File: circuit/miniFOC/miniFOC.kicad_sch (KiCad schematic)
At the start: 0 parts

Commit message: The design of the miniFOC circuit schematic is basically completed.
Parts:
- added C?: 22uF, Capacitor_SMD:C_0603_1608Metric_Pad1.08x0.95mm_HandSolder, symbol Device:C
- added C? (x4): 330pF, Capacitor_SMD:C_0402_1005Metric, symbol Device:C
- added C? (x3): 1uF, Capacitor_SMD:C_0402_1005Metric, symbol Device:C
- added C?: 4.7uF, Capacitor_SMD:C_1206_3216Metric_Pad1.33x1.80mm_HandSolder, symbol Device:C
- added C?: 100nF, Capacitor_SMD:C_0603_1608Metric_Pad1.08x0.95mm_HandSolder, symbol Device:C
- added C?: 10uF, Capacitor_SMD:C_1206_3216Metric_Pad1.33x1.80mm_HandSolder, symbol Device:C
- added C? (x2): 10uF, Capacitor_SMD:C_0603_1608Metric_Pad1.08x0.95mm_HandSolder, symbol Device:C
- added C?: 100nF, Capacitor_SMD:C_0402_1005Metric, symbol Device:C
- added D? (x3): B0530W, Diode_SMD:D_SOD-123, symbol Diode:1N4148W
- added L?: 4.7uH, PowerLibrary:IND-SMD_L4.6-W4.2_SMMS0420, symbol Device:L
- added Q? (x6): AP30H50Q, Package_SON:VSON-8_3.3x3.3mm_P0.65mm_NexFET, symbol Library:AP30H50Q
- added R? (x2): 20mR, Resistor_SMD:R_0805_2012Metric, symbol Device:R
- added R? (x4): 1kR, Resistor_SMD:R_0402_1005Metric, symbol Device:R
- added R? (x4): 15kR, Resistor_SMD:R_0402_1005Metric, symbol Device:R
- added R?: 100kR, Resistor_SMD:R_0603_1608Metric_Pad0.98x0.95mm_HandSolder, symbol Device:R
- added R?: 10kR, Resistor_SMD:R_0402_1005Metric, symbol Device:R
- added R?: 3kR, Resistor_SMD:R_0603_1608Metric_Pad0.98x0.95mm_HandSolder, symbol Device:R
- added R?: 16kR, Resistor_SMD:R_0603_1608Metric_Pad0.98x0.95mm_HandSolder, symbol Device:R
- added U?: COS722MR, Package_SO:MSOP-8_3x3mm_P0.65mm, symbol Library:COS722MR
- added U?: AT32F421C8, Package_QFP:LQFP-48_7x7mm_P0.5mm, symbol Library:AT32F421C8
- added U?: EG2133, Package_SO:TSSOP-20_4.4x6.5mm_P0.65mm, symbol Library:EG2133
- added U?: JW5017S, Package_TO_SOT_SMD:SOT-23-6, symbol power_Library:JW5017S
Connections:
- new net: C?.1, R?.1, R?.2, U?.5 (IN2+)
- new net: C?.1, R?.1, R?.1, U?.3 (IN1+)
- new net: C?.2, R?.2, R?.2, U?.2 (IN1-)
- new net: C?.1, L?.1, U?.6 (SW)
- new net: C?.2, U?.1 (BST)
- new net: R?.1, U?.4 (EN)
- new net: C?.2, R?.1, R?.2, U?.6 (IN2-)
- new net: R?.2, R?.2, U?.3 (FB)
- new net +15V: C?.2, C?.2, Q?.5 (D), Q?.5 (D), Q?.5 (D), R?.2, U?.5 (VIN)
- new net +3.3V: R?.1, U?.1 (VDD), U?.24 (VDD), U?.48 (VDD), U?.9 (VDDA)
- new net +5V: C?.2, C?.2, C?.2, D?.2 (A), D?.2 (A), D?.2 (A), L?.2, R?.1, U?.7 (VCC), U?.8 (VDD)
- new net ADC1_CH0: C?.1, R?.1, U?.1 (OUTA), U?.10 (PA0)
- new net ADC1_CH1: C?.1, R?.1, U?.11 (PA1), U?.7 (OUTB)
- new net ADC1_CH2: U?.12 (PA2)
- new net GND: C?.1, C?.1, C?.1, C?.1, C?.1, C?.2, Q?.1 (S), Q?.2 (S), Q?.3 (S), R?.1, R?.1, R?.2, R?.2, R?.2, U?.2 (GND), U?.23 (VSS), U?.4 (VSS), U?.47 (VSS), U?.8 (GND), U?.8 (VSSA)
- new net HO1: Q?.4 (G), U?.19 (HO1)
- new net HO2: Q?.4 (G), U?.16 (HO2)
- new net HO3: Q?.4 (G), U?.13 (HO3)
- new net LO1: Q?.4 (G), U?.11 (LO1)
- new net LO2: Q?.4 (G), U?.10 (LO2)
- new net LO3: Q?.4 (G), U?.9 (LO3)
- new net NRST: C?.1, R?.2, U?.7 (NRST)
- new net SA1_P: Q?.1 (S), Q?.2 (S), Q?.3 (S), R?.1, R?.2
- new net SA2_P: Q?.1 (S), Q?.2 (S), Q?.3 (S), R?.1, R?.1
- new net SPI_CLK: U?.15 (PA5)
- new net SPI_CS: U?.14 (PA4)
- new net SPI_MISO: U?.16 (PA6)
- new net SWDCLK: U?.37 (SWCLK)
- new net SWDIO: U?.34 (SWDIO)
- new net TIM1_CH1: U?.1 (HIN1), U?.29 (PA8), U?.4 (~{LIN1})
- new net TIM1_CH2: U?.2 (HIN2), U?.30 (PA9), U?.5 (~{LIN2})
- new net TIM1_CH3: U?.3 (HIN3), U?.31 (PA10), U?.6 (~{LIN3})
- new net USART1_RX: U?.43 (PB7)
- new net USART1_TX: U?.42 (PB6)
- new net VAA: C?.2, C?.2, R?.2, R?.2
- new net VB1: C?.1, D?.1 (K), U?.20 (VB1)
- new net VB2: C?.1, D?.1 (K), U?.17 (VB2)
- new net VB3: C?.1, D?.1 (K), U?.14 (VB3)
- new net VS1: C?.2, Q?.1 (S), Q?.2 (S), Q?.3 (S), Q?.5 (D), U?.18 (VS1)
- new net VS2: C?.2, Q?.1 (S), Q?.2 (S), Q?.3 (S), Q?.5 (D), U?.15 (VS2)
- new net VS3: C?.2, Q?.1 (S), Q?.2 (S), Q?.3 (S), Q?.5 (D), U?.12 (VS3)
- no-connect marks 0 -> 27
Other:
- note added: "Driver"
- note added: "MCU"
- note added: "Power"
- note added: "Sample"

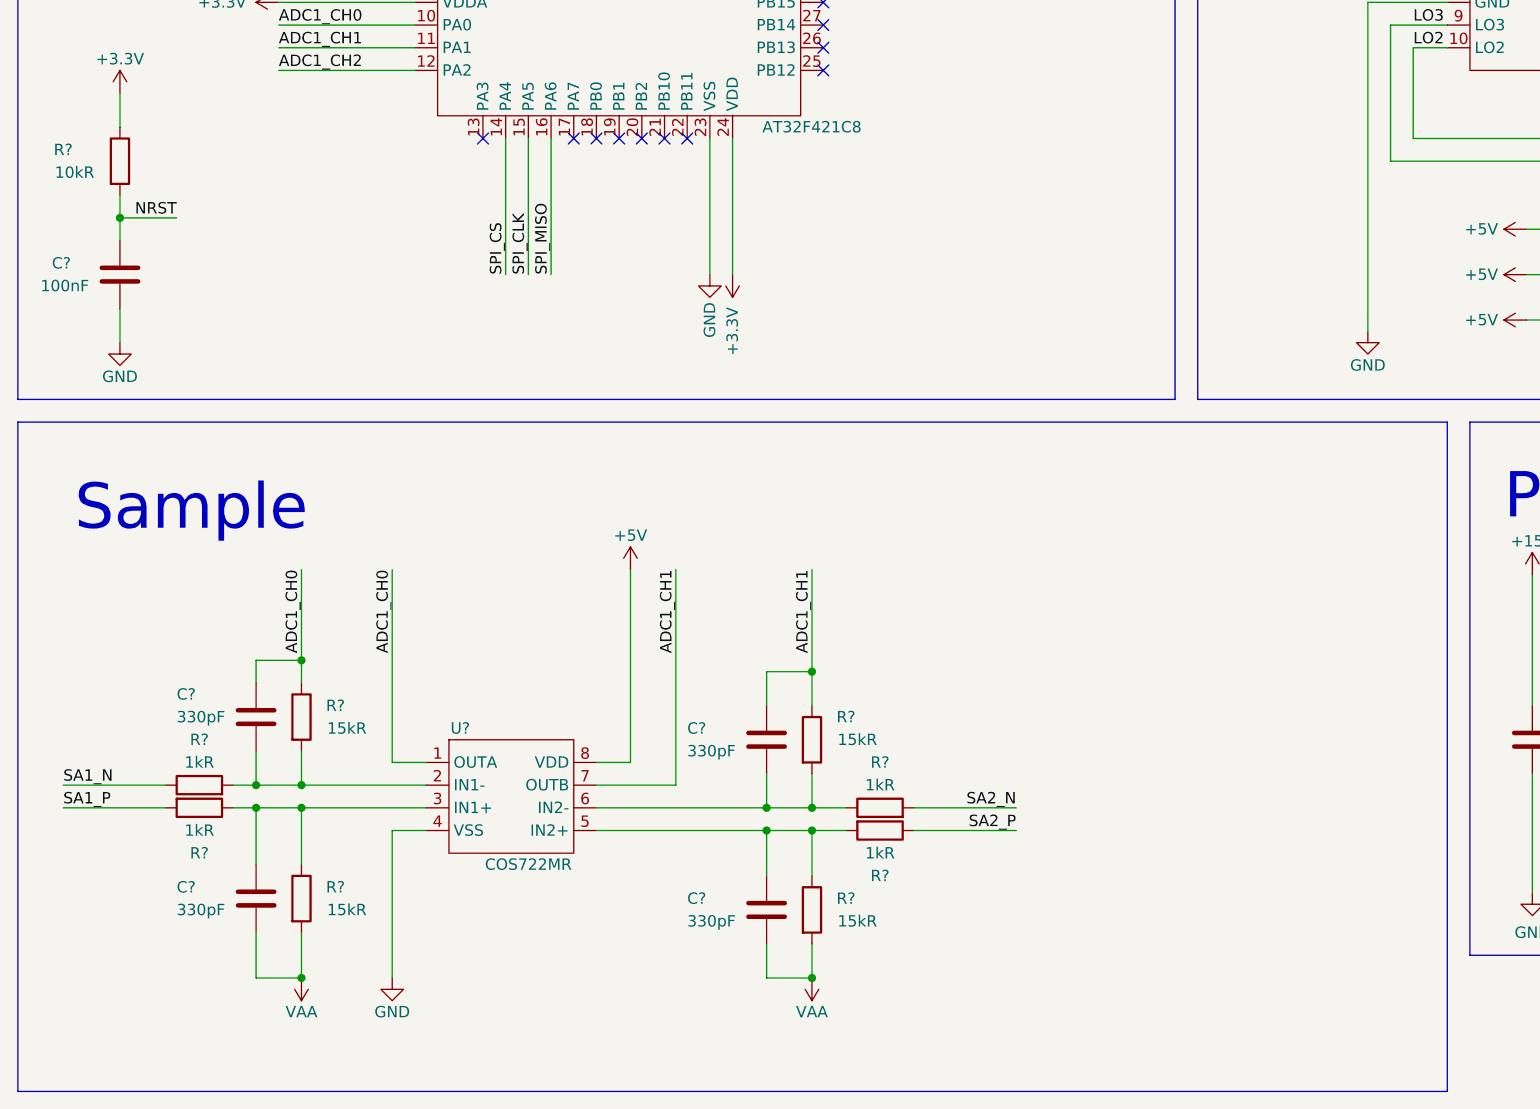
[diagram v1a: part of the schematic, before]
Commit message: Modify the op-amp symbol to triangle.
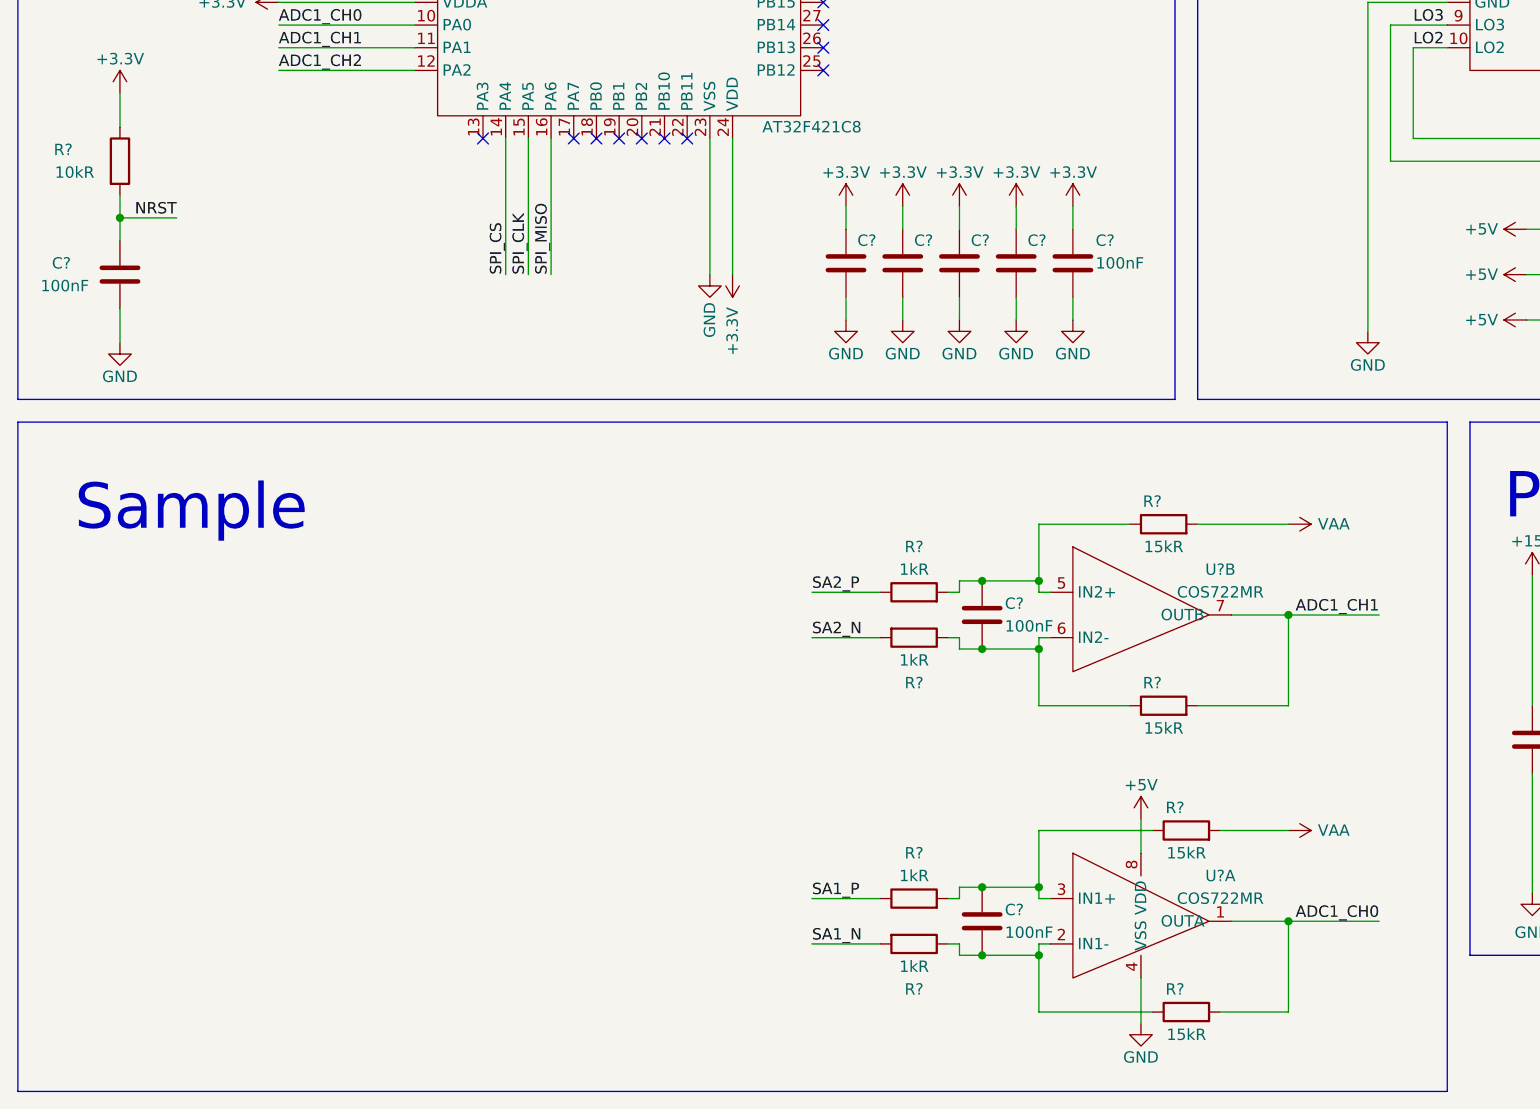
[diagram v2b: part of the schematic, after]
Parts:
- removed C? (x4): 330pF, Capacitor_SMD:C_0402_1005Metric, symbol Device:C
- removed R? (x2): 1kR, Resistor_SMD:R_0402_1005Metric, symbol Device:R
- removed R? (x3): 15kR, Resistor_SMD:R_0402_1005Metric, symbol Device:R
- removed U?: COS722MR, Package_SO:MSOP-8_3x3mm_P0.65mm, symbol Library:COS722MR
- added C? (x7): 100nF, Capacitor_SMD:C_0402_1005Metric, symbol Device:C
- added R? (x3): 15kR, Resistor_SMD:R_0402_1005Metric, symbol Device:R
- added R? (x2): 1kR, Resistor_SMD:R_0402_1005Metric, symbol Device:R
- added U? (x2): COS722MR, Package_SO:MSOP-8_3x3mm_P0.65mm, symbol Library:COS722MR
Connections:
- net +3.3V: now also C?.1, C?.1, C?.1, C?.1, C?.1
- net +5V: now also U?.8 (VDD)
- net ADC1_CH0: now also R?.2, U?.1 (OUTA)
- net ADC1_CH1: now also R?.2, U?.7 (OUTB)
- net GND: now also R?.2, C?.2, C?.2, C?.2, C?.2, C?.2, R?.2, U?.4 (VSS); no longer R?.1
- net SA1_P: now also R?.1; no longer R?.2
- net SA2_P: now also R?.1
- net VAA: now also R?.2, R?.2; no longer R?.2
- net at R?.1, R?.1: now also C?.2, U?.2 (IN1-)
- net at R?.2: now also C?.1, R?.1, U?.3 (IN1+)
- new net: C?.1, R?.1, R?.2, U?.5 (IN2+)
- new net: C?.2, R?.1, R?.1, U?.6 (IN2-)
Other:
- moved on the sheet: R?

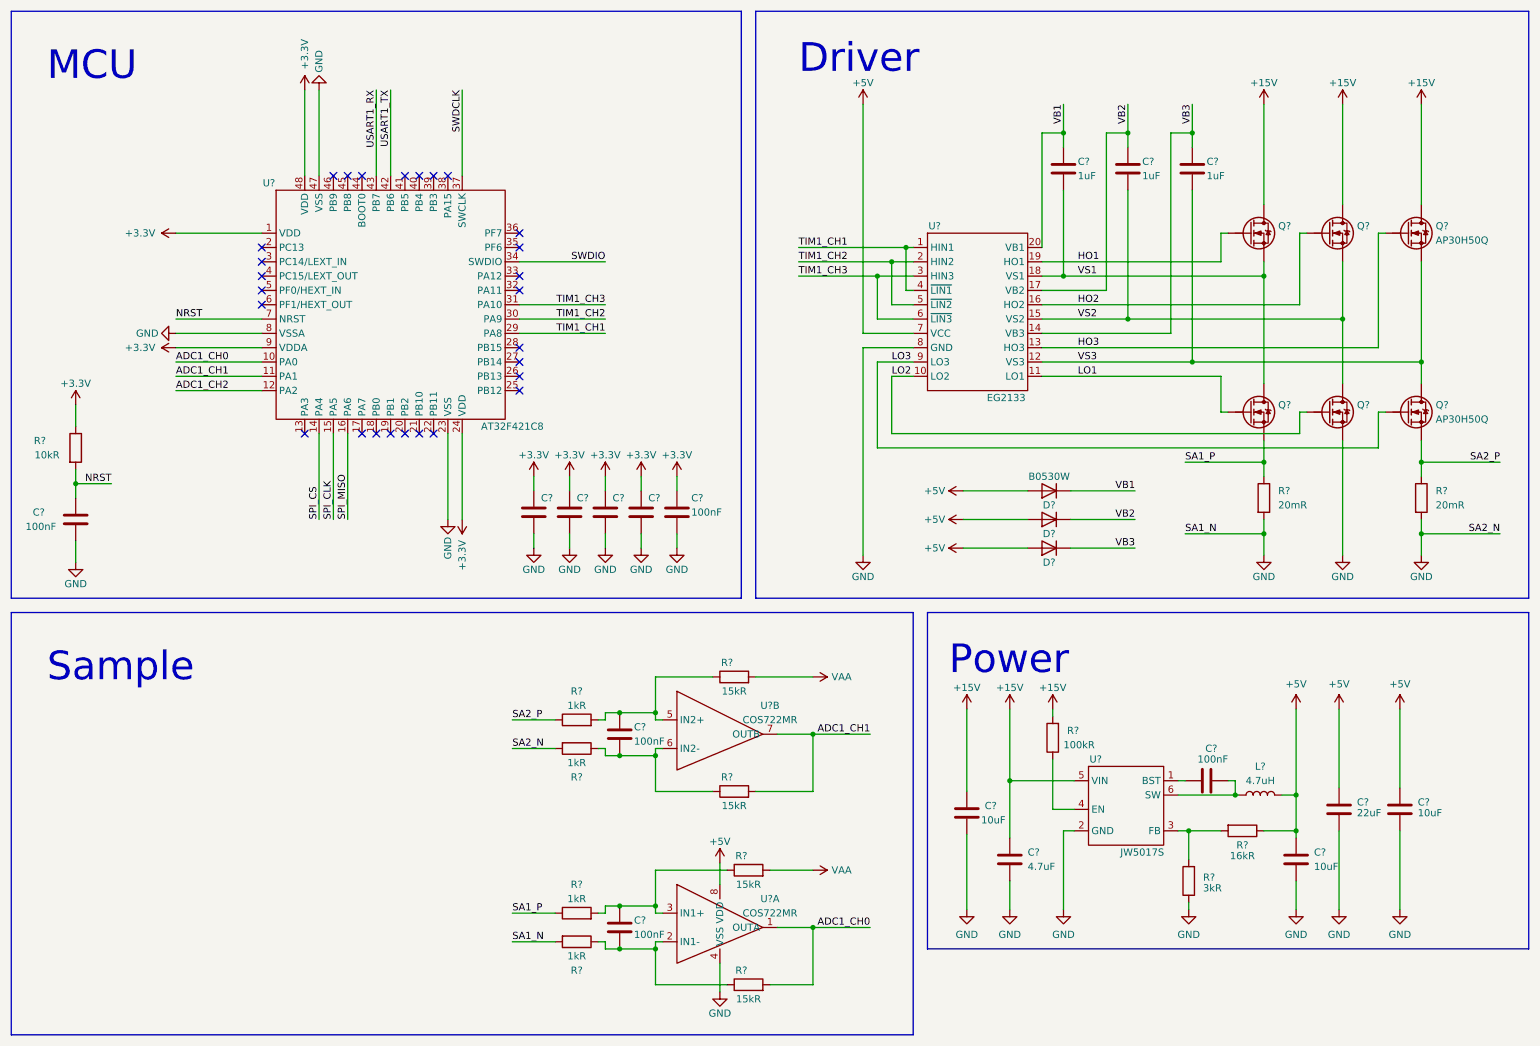
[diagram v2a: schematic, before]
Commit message: Finished new miniFOC schematic design.
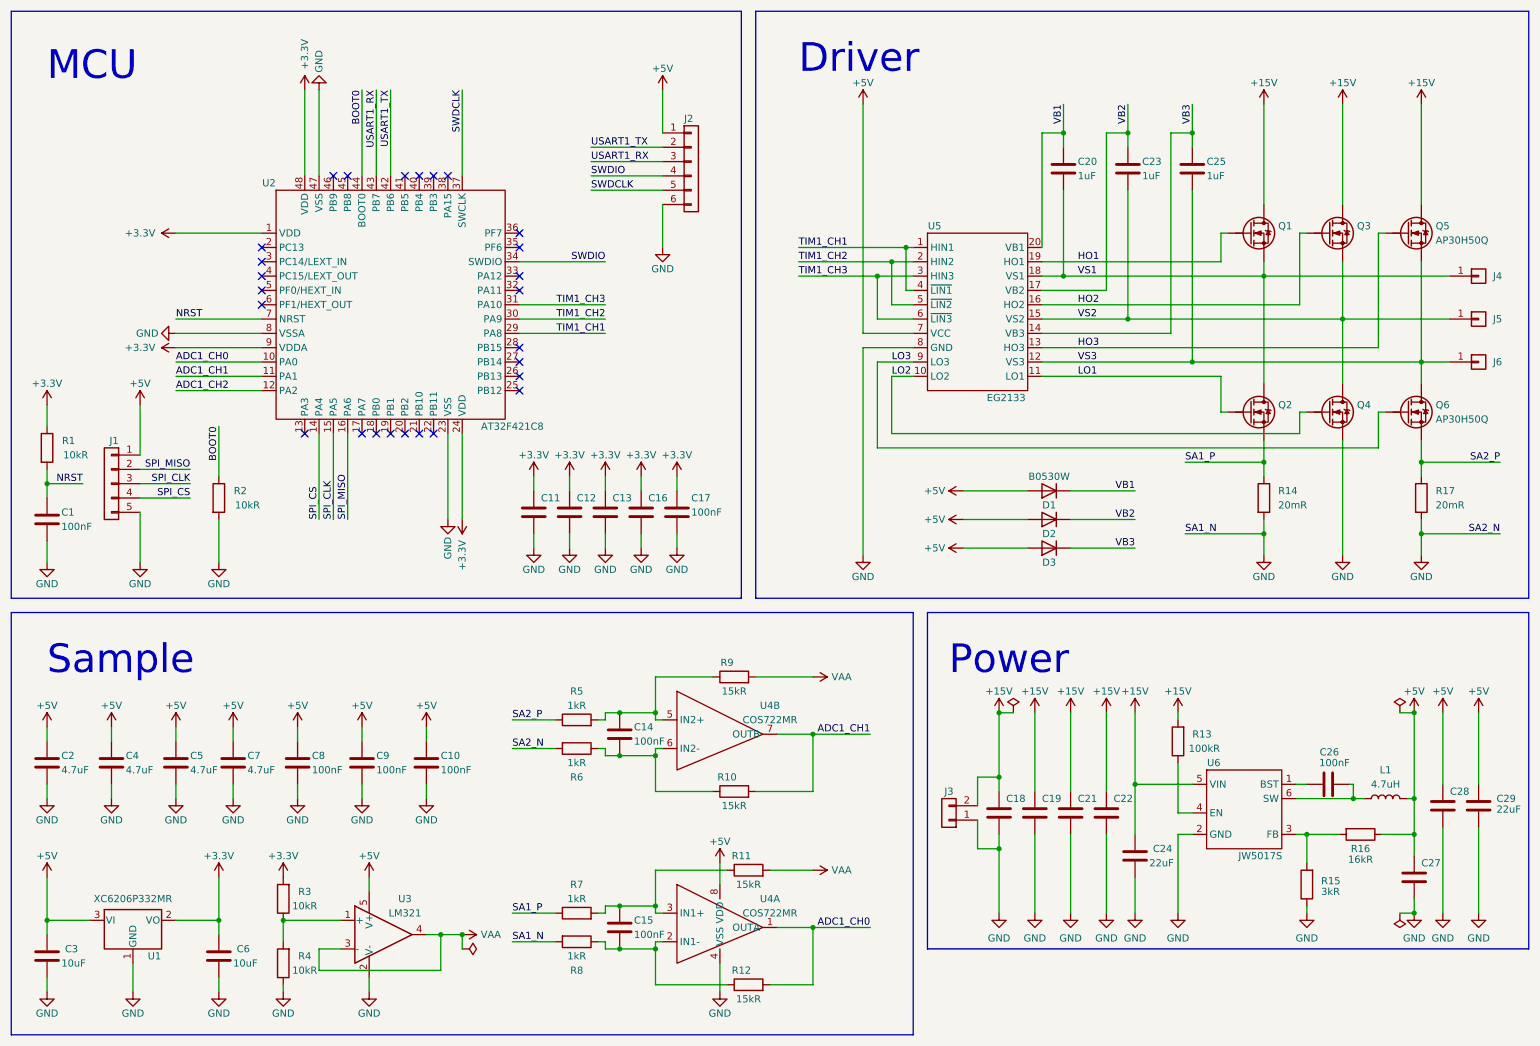
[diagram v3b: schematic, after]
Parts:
- removed C?: 4.7uF, Capacitor_SMD:C_1206_3216Metric_Pad1.33x1.80mm_HandSolder, symbol Device:C
- added C10, C8, C9: 100nF, Capacitor_SMD:C_0402_1005Metric, symbol Device:C
- added C18, C19, C21, C24: 22uF, Capacitor_SMD:C_0805_2012Metric, symbol Device:C
- added C2, C4, C5, C7: 4.7uF, Capacitor_SMD:C_0402_1005Metric, symbol Device:C
- added C3, C6: 10uF, Capacitor_SMD:C_1206_3216Metric_Pad1.33x1.80mm_HandSolder, symbol Device:C
- added J1: Conn_01x05, Connector_JST:JST_GH_SM05B-GHS-TB_1x05-1MP_P1.25mm_Horizontal, symbol Connector_Generic:Conn_01x05
- added J2: Conn_01x06, symbol Connector_Generic:Conn_01x06
- added J3: Conn_01x02, symbol Connector_Generic:Conn_01x02
- added J4, J5, J6: Conn_01x01, symbol Connector_Generic:Conn_01x01
- added R2, R3, R4: 10kR, Resistor_SMD:R_0402_1005Metric, symbol Device:R
- added U1: XC6206P332MR, Package_TO_SOT_SMD:SOT-23, symbol Regulator_Linear:XC6206PxxxMR
- added U3: LM321, Package_TO_SOT_SMD:SOT-23-5, symbol Amplifier_Operational:LM321
- C22: renamed from C?; value 10uF -> 22uF; footprint Capacitor_SMD:C_1206_3216Metric_Pad1.33x1.80mm_HandSolder -> Capacitor_SMD:C_0805_2012Metric
- C27, C29: renamed from C?; value 10uF -> 22uF
- gave numbers to parts that had none: 41
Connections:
- net +15V: now also C18.2, C19.2, C21.2, C24.2, J3.2 (Pin_2)
- net +3.3V: now also C6.2, R3.2, U1.2 (VO)
- net +5V: now also C10.1, C2.1, C3.2, C4.1, C5.1, C7.1, C8.1, C9.1, J1.1 (Pin_1), J2.1 (Pin_1), U1.3 (VI), U3.5 (V+)
- net GND: now also C10.2, C18.1, C19.1, C2.2, C21.1, C24.1, C3.1, C4.2, C5.2, C6.1, C7.2, C8.2, C9.2, J1.5 (Pin_5), J2.6 (Pin_6), J3.1 (Pin_1), R2.2, R4.1, U1.1 (GND), U3.2 (V-)
- net SPI_CLK: now also J1.3 (Pin_3)
- net SPI_CS: now also J1.4 (Pin_4)
- net SPI_MISO: now also J1.2 (Pin_2)
- net SWDCLK: now also J2.5 (Pin_5)
- net SWDIO: now also J2.4 (Pin_4)
- net USART1_RX: now also J2.3 (Pin_3)
- net USART1_TX: now also J2.2 (Pin_2)
- net VAA: now also U3.3 (-), U3.4
- net VS1: now also J4.1 (Pin_1)
- net VS2: now also J5.1 (Pin_1)
- net VS3: now also J6.1 (Pin_1)
- net BOOT0: now reaches U2.44 (BOOT0)
- net BOOT0: now also R2.1
- new net: R3.1, R4.2, U3.1 (+)
- no-connect marks 27 -> 26
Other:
- moved on the sheet: C1, C22, C26, C27, C28, C29, L1, R1, R13, R15, R16, U6
